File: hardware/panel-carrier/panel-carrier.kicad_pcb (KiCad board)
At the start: 2 copper layers, 80 x 62 mm, 20 parts, among them J1 display P3: IO6 IO7 IO15 IO16, J2 display P4: GND 3.3V IO17 IO18, J3 LINK to motion: GND TX RX, J4 MPG +5V GND A B, J5 5V IN from buck, J6 BUTTONS A0-A6, COM, J7 ROUTER LED + -, U1 74LVC14, U2 MCP23017 @0x20

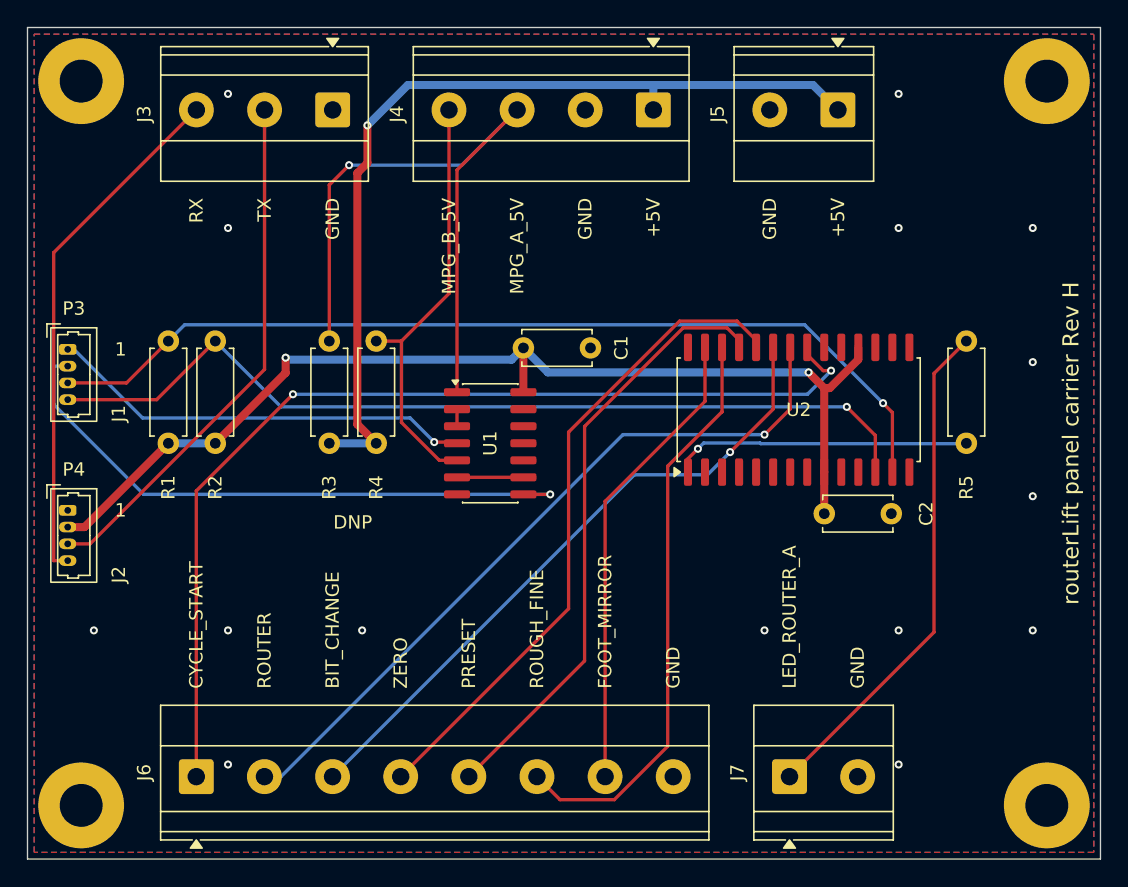
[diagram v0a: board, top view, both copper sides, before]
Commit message: fix(hardware): rectangular motion holes, shared link labels, regenerate boards
- motion carrier: M3 holes (4,4) (93,4) (4,56.5) (93,56.5), 89 x 52.5 mm, asserted
  as a rectangle, >=4 mm from edges, clear of courtyards/text, >=10 mm from the
  antenna keep-out; pitch silkscreen; DRV_ALM block lifted 7.5 mm; J2 refdes moved
  below its tail
- J8 and panel J3 labelled GND / LINK_TX / LINK_RX with a straight-through note;
  panel R1-R5 moved down 1 mm to make room
- stitch-avoid is builder state on both boards
- README: hole coordinates and pitch, Freerouting version override, what
  regeneration overwrites

Co-Authored-By: Claude Opus 5 (1M context) <noreply@anthropic.com>
Claude-Session: https://claude.ai/code/session_01N1nWXzYgvFT6pqfHGhLK6P
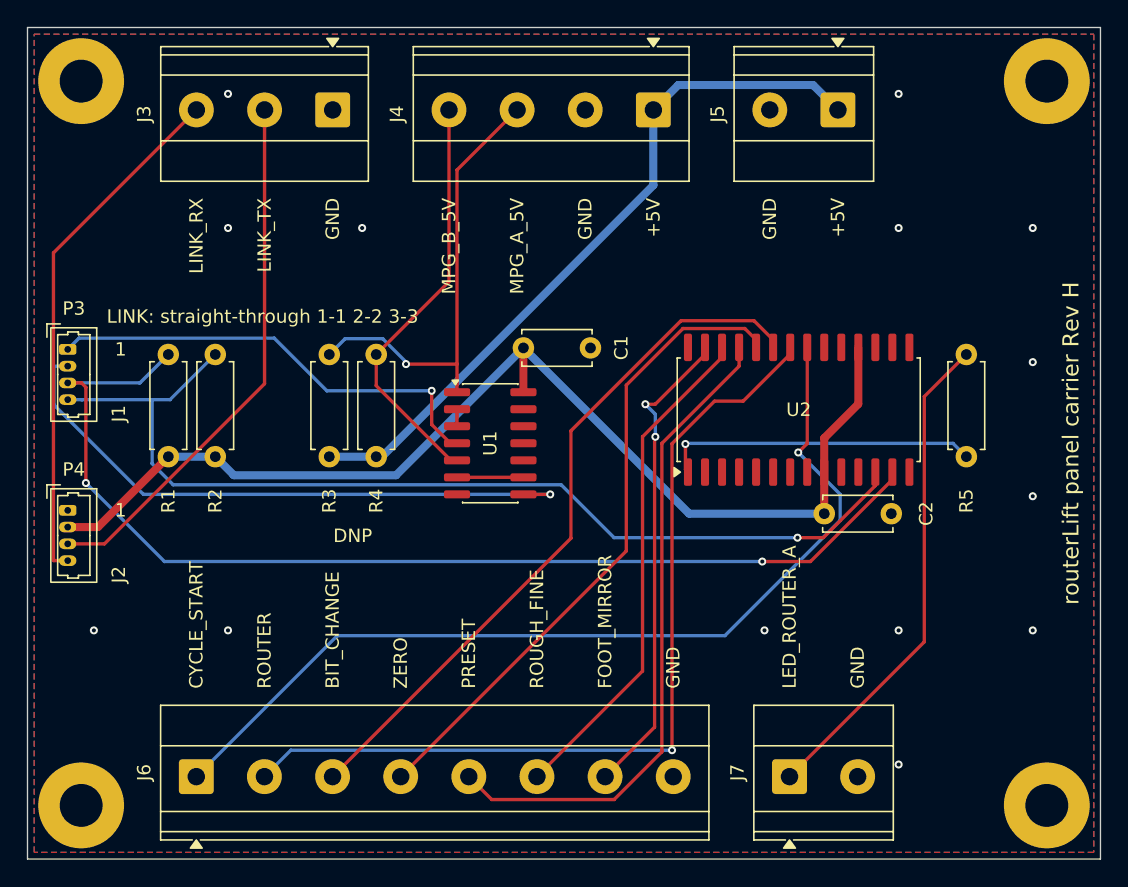
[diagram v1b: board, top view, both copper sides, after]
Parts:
- moved R1 1.00 mm to (110.5, 132.0)
- moved R2 1.00 mm to (114.0, 132.0)
- moved R3 1.00 mm to (122.5, 132.0)
- moved R4 1.00 mm to (126.0, 132.0)
- moved R5 1.00 mm to (170.0, 132.0)
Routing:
- net /MPG_A_5V: track 50.9 -> 33.8 mm
- net +5V: track 67.0 -> 53.5 mm, vias 1 -> 0
- net /SDA: track 70.4 -> 82.6 mm, vias 1 -> 2
- net /BTN_ROUTER: track 55.1 -> 66.1 mm
- net /SCL: track 67.7 -> 76.0 mm
- net /SW_ROUGH_FINE: track 43.5 -> 37.7 mm
- net /BTN_CYCLE_START: track 75.2 -> 70.4 mm, vias 2 -> 1
- net +3V3: track 81.0 -> 85.0 mm, vias 2 -> 0
- net /BTN_BIT_CHANGE: track 48.8 -> 52.8 mm, vias 1 -> 0
- net /BTN_PRESET: track 45.2 -> 49.1 mm
- net /MPG_A_3V3: track 31.9 -> 34.1 mm
- net /LED_ROUTER_DRV: track 22.3 -> 23.6 mm
- net /FOOT_MIRROR: track 35.1 -> 36.1 mm, vias 0 -> 2
- net /LED_ROUTER_A: track 37.9 -> 36.9 mm
- net /BTN_ZERO: track 49.4 -> 48.5 mm
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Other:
- board text added: "LINK: straight-through 1-1 2-2 3-3"
- board text added: "LINK_RX"
- board text added: "LINK_TX"
- board text removed: "RX"
- board text removed: "TX"
